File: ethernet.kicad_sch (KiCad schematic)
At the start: 20 parts, among them U6 RTL8211F-CG

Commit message: sch-eth-usb-updated
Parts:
- added C809: 4u7, Capacitor_SMD:C_0402_1005Metric, symbol Device:C
- added C810, C811: 100n, Capacitor_SMD:C_0402_1005Metric, symbol Device:C
- added J800: HR911130A, HR911130A, symbol Schematic-Lib-PhilsLab:HR911130A
- added L800: 3uh3, Inductor_SMD:L_0603_1608Metric, symbol Device:L
- added R800, R801, R804, R818, R819, R820: 4K7, Resistor_SMD:R_0402_1005Metric, symbol Device:R
- added R802: DNP_4K7, Resistor_SMD:R_0402_1005Metric, symbol Device:R
- added R803, R805, R806, R813, R814: 1k, Resistor_SMD:R_0402_1005Metric, symbol Device:R
- added R807, R808, R809, R810, R811, R812, R815, R816, R817: 22R, Resistor_SMD:R_0402_1005Metric, symbol Device:R
- added R821: 2K49, Resistor_SMD:R_0402_1005Metric, symbol Device:R
- added R822, R823: 510, Resistor_SMD:R_0402_1005Metric, symbol Device:R
- added X800: ECS-2520MV-250, XTAL_2520, symbol Schematic-Lib-PhilsLab:ECS-2520MV-130-BN-TR
- renumbered U6 to U800
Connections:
- net +1V0_ETH: now also C809.1, C810.1, L800.2
- net +1V8_ETH: now also C811.1, R800.2, R801.2, R802.2, R804.2, R813.2, R814.2, X800.1 (EN), X800.4 (VDD)
- net +3V3: now also J800.11 (LED_GREEN_A), J800.14 (LED_YELLOW_A), R818.1, R820.1
- net GND: now also C809.2, C810.2, C811.2, J800.10 (GND), R803.1, R805.1, R806.1, R816.2, R819.2, R821.2, X800.2 (GND)
- net MDI0_P: now reaches U800.1 (MDIP0)
- net MDI0_P: now also J800.2 (MD0+)
- net MDI3_N: now reaches U800.10 (MDIN3)
- net MDI3_N: now also J800.9 (MD3-)
- net ETH_NRST_+3V3: now reaches U800.12 (PHYRSTB)
- net ETH_MDC: now reaches U800.13 (MDC)
- net ETH_MDIO: now reaches U800.14 (MDIO)
- net ETH_MDIO: now also R814.1
- net ETH_PHY_TXD3: now reaches U800.15 (TXD3)
- net ETH_PHY_TXD2: now reaches U800.16 (TXD2)
- net ETH_PHY_TXD1: now reaches U800.17 (TXD1)
- net ETH_PHY_TXD0: now reaches U800.18 (TXD0)
- net ETH_PHY_TXCTL: now reaches U800.19 (TXCTL)
- net MDI0_N: now reaches U800.2 (MDIN0)
- net MDI0_N: now also J800.3 (MD0-)
- net ETH_PHY_TXCLK: now reaches U800.20 (TXC)
- net ETH_PHY_RXD3: now reaches U800.22 (RXD3/PHYAD0)
- net ETH_PHY_RXD3: now also R810.1
- net ETH_PHY_RXD2: now reaches U800.23 (RXD2/PLLOFF)
- net ETH_PHY_RXD2: now also R809.1
- net ETH_PHY_RXD1: now reaches U800.24 (RXD1/TXDLY)
- net ETH_PHY_RXD1: now also R808.1
- net ETH_PHY_RXD0: now reaches U800.25 (RXD0/RXDLY)
- net ETH_PHY_RXD0: now also R807.1
- net ETH_PHY_RXCTL: now reaches U800.26 (RXCTL/PHYAD2)
- net ETH_PHY_RXCTL: now also R811.1
- net ETH_PHY_RXCLK: now reaches U800.27 (RXC/PHYAD1)
- net ETH_PHY_RXCLK: now also R812.1
- net at U800.30 (REG_OUT/LDO_OUT): now also L800.1
- net ETH_NINT: now reaches U800.31 (INTB/PMEB)
- net ETH_NINT: now also R813.1
- net ETH_LED0: now reaches U800.32 (LED0/CFG_EXT)
- net ETH_LED0: now also R818.2, R822.2
- net ETH_LED1: now reaches U800.33 (LED1/CFG_LDO0)
- net ETH_LED1: now also R819.1
- net ETH_LED2: now reaches U800.34 (LED2/CFG_LDO1)
- net ETH_LED2: now also R820.2, R823.2
- net ETH_CLKOUT: now reaches U800.35 (CLKOUT)
- net ETH_CLKOUT: now also R817.1
- net at U800.36 (XTAL_IN): now also R816.1
- net ETH_CLK_25MHZ: now reaches U800.37 (XTAL_OUT/EXT_CLK)
- net ETH_CLK_25MHZ: now also R815.1
- net ETH_RSET: now reaches U800.39 (RSET)
- net ETH_RSET: now also R821.1
- net MDI1_P: now reaches U800.4 (MDIP1)
- net MDI1_P: now also J800.4 (MD1+)
- net MDI1_N: now reaches U800.5 (MDIN1)
- net MDI1_N: now also J800.7 (MD1-)
- net MDI2_P: now reaches U800.6 (MDIP2)
- net MDI2_P: now also J800.5 (MD2+)
- net MDI2_N: now reaches U800.7 (MDIN2)
- net MDI2_N: now also J800.6 (MD2-)
- net MDI3_P: now reaches U800.9 (MDIP3)
- net MDI3_P: now also J800.8 (MD3+)
- new net CGND: J800.SH (SHIELD)
- new net CLK_25MHZ: R815.2, X800.3 (OUT)
- new net ETH_LED_GR_K: J800.12 (LED_GREEN_K), R822.1
- new net ETH_LED_YL_A: J800.13 (LED_YELLOW_K), R823.1
- new net ETH_RXCLK: R806.2, R812.2
- new net ETH_RXCTL: R805.2, R811.2
- new net ETH_RXD0: R800.1, R807.2
- new net ETH_RXD1: R801.1, R808.2
- new net ETH_RXD2: R802.1, R803.2, R809.2
- new net ETH_RXD3: R804.1, R810.2
- new net PL_CLK_125MHZ: R817.2
- no-connect marks 0 -> 1
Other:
- note added: "Diff pair"
- note added: "GIGABIT ETHERNET"
- moved on the sheet: C807, C808

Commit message: all page
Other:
- title: (none) -> (text "GIGABIT ETHERNET" (exclude_from_sim no)
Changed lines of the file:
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@@
 	(generator_version "8.0")
 	(paper "A4")
+	(title_block
+		(title "(text \"GIGABIT ETHERNET\" (exclude_from_sim no)")
+		(date "2024-12-05")
+	)
 	(junction
 		(at 166.37 58.42)
@@
 	(wire
 		(pts
+			(xy 82.55 116.84) (xy 107.95 116.84)
+		)
+		(stroke
+			(width 0)
+			(type default)
+		)
+	)
+	(wire
+		(pts
 			(xy 276.86 71.12) (xy 276.86 111.76)
 		)
@@
 		(pts
 			(xy 29.21 71.12) (xy 50.8 71.12)
-		)
-		(stroke
-			(width 0)
-			(type default)
-		)
-	)
-	(wire
-		(pts
-			(xy 85.09 116.84) (xy 107.95 116.84)
 		)
 		(stroke
@@
 		)
 	)
-	(label "ETH_NRST_+3V3"
-		(at 85.09 116.84 0)
-		(fields_autoplaced yes)
-		(effects
-			(font
-				(size 1.016 1.016)
-				(thickness 0.127)
-			)
-			(justify left bottom)
-		)
-	)
 	(label "ETH_LED_GR_K"
 		(at 243.84 111.76 0)
@@
 		)
 	)
+	(global_label "ETH_NRST_+3V3"
+		(shape input)
+		(at 82.55 116.84 180)
+		(fields_autoplaced yes)
+		(effects
+			(font
+				(size 1.016 1.016)
+				(thickness 0.254)
+				(bold yes)
+			)
+			(justify right)
+		)
+		(property "Intersheetrefs" "${INTERSHEET_REFS}"
+			(at 67.3351 116.84 0)
+			(effects
+				(font
+					(size 1.27 1.27)
+				)
+				(justify right)
+				(hide yes)
+			)
+		)
+	)

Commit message: all page
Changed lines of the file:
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@@
 	(wire
 		(pts
-			(xy 88.9 96.52) (xy 107.95 96.52)
+			(xy 99.06 96.52) (xy 107.95 96.52)
 		)
 		(stroke
@@
 	(wire
 		(pts
-			(xy 88.9 93.98) (xy 107.95 93.98)
+			(xy 99.06 93.98) (xy 107.95 93.98)
 		)
 		(stroke
@@
 	(wire
 		(pts
-			(xy 88.9 88.9) (xy 107.95 88.9)
+			(xy 99.06 88.9) (xy 107.95 88.9)
 		)
 		(stroke
@@
 	(wire
 		(pts
-			(xy 88.9 86.36) (xy 107.95 86.36)
+			(xy 99.06 86.36) (xy 107.95 86.36)
 		)
 		(stroke
@@
 	(wire
 		(pts
-			(xy 73.66 129.54) (xy 91.44 129.54)
+			(xy 80.01 129.54) (xy 91.44 129.54)
 		)
 		(stroke
@@
 	(wire
 		(pts
-			(xy 88.9 91.44) (xy 107.95 91.44)
+			(xy 99.06 91.44) (xy 107.95 91.44)
 		)
 		(stroke
@@
 	(wire
 		(pts
-			(xy 88.9 99.06) (xy 107.95 99.06)
+			(xy 99.06 99.06) (xy 107.95 99.06)
 		)
 		(stroke
@@
 		)
 	)
-	(label "ETH_PHY_TXCTL"
-		(at 88.9 96.52 0)
-		(fields_autoplaced yes)
-		(effects
-			(font
-				(size 1.016 1.016)
-				(thickness 0.127)
-			)
-			(justify left bottom)
-		)
-	)
 	(label "ETH_NINT"
 		(at 85.09 111.76 0)
@@
 		)
 	)
-	(label "ETH_PHY_TXD3"
-		(at 88.9 93.98 0)
-		(fields_autoplaced yes)
-		(effects
-			(font
-				(size 1.016 1.016)
-			)
-			(justify left bottom)
-		)
-	)
-	(label "ETH_PHY_TXD2"
-		(at 88.9 91.44 0)
-		(fields_autoplaced yes)
-		(effects
-			(font
-				(size 1.016 1.016)
-			)
-			(justify left bottom)
-		)
-	)
 	(label "MDI2_N"
 		(at 191.77 86.36 0)
@@
 		)
 	)
-	(label "ETH_PHY_TXD1"
-		(at 88.9 88.9 0)
-		(fields_autoplaced yes)
-		(effects
-			(font
-				(size 1.016 1.016)
-			)
-			(justify left bottom)
-		)
-	)
 	(label "ETH_LED_GR_K"
 		(at 243.84 111.76 0)
@@
 		)
 	)
-	(label "PL_CLK_125MHZ"
-		(at 73.66 129.54 0)
-		(fields_autoplaced yes)
-		(effects
-			(font
-				(size 1.016 1.016)
-				(thickness 0.127)
-			)
-			(justify left bottom)
-		)
-	)
 	(label "MDI1_P"
 		(at 191.77 76.2 0)
@@
 		)
 	)
-	(label "ETH_PHY_TXD0"
-		(at 88.9 86.36 0)
-		(fields_autoplaced yes)
-		(effects
-			(font
-				(size 1.016 1.016)
-			)
-			(justify left bottom)
-		)
-	)
-	(label "ETH_PHY_TXCLK"
-		(at 88.9 99.06 0)
-		(fields_autoplaced yes)
-		(effects
-			(font
-				(size 1.016 1.016)
-				(thickness 0.127)
-			)
-			(justify left bottom)
-		)
-	)
 	(label "ETH_RXD0"
 		(at 29.21 68.58 0)
@@
 		)
 	)
-	(label "ETH_MDC"
-		(at 90.17 106.68 0)
-		(fields_autoplaced yes)
-		(effects
-			(font
-				(size 1.016 1.016)
-				(thickness 0.127)
-			)
-			(justify left bottom)
-		)
-	)
 	(label "ETH_LED1"
 		(at 190.5 109.22 0)
@@
 			)
 			(justify left bottom)
+		)
+	)
+	(global_label "PL_CLK_125MHZ"
+		(shape input)
+		(at 80.01 129.54 180)
+		(fields_autoplaced yes)
+		(effects
+			(font
+				(size 1.016 1.016)
+				(thickness 0.254)
+				(bold yes)
+			)
+			(justify right)
+		)
+		(property "Intersheetrefs" "${INTERSHEET_REFS}"
+			(at 64.65 129.54 0)
+			(effects
+				(font
+					(size 1.27 1.27)
+				)
+				(justify right)
+				(hide yes)
+			)
+		)
+	)
+	(global_label "ETH_PHY_TXCTL"
+		(shape input)
+		(at 99.06 96.52 180)
+		(fields_autoplaced yes)
+		(effects
+			(font
+				(size 0.762 0.762)
+				(thickness 0.254)
+				(bold yes)
+			)
+			(justify right)
+		)
+		(property "Intersheetrefs" "${INTERSHEET_REFS}"
+			(at 88.0839 96.52 0)
+			(effects
+				(font
+					(size 1.27 1.27)
+				)
+				(justify right)
+				(hide yes)
+			)
+		)
+	)
+	(global_label "ETH_MDC"
+		(shape input)
+		(at 90.17 106.68 180)
+		(fields_autoplaced yes)
+		(effects
+			(font
+				(size 0.762 0.762)
+				(thickness 0.254)
+				(bold yes)
+			)
+			(justify right)
+		)
+		(property "Intersheetrefs" "${INTERSHEET_REFS}"
+			(at 82.8588 106.68 0)
+			(effects
+				(font
+					(size 1.27 1.27)
+				)
+				(justify right)
+				(hide yes)
+			)
+		)
+	)
+	(global_label "ETH_PHY_TXD1"
+		(shape input)
+		(at 99.06 88.9 180)
+		(fields_autoplaced yes)
+		(effects
+			(font
+				(size 0.762 0.762)
+				(thickness 0.254)
+				(bold yes)
+			)
+			(justify right)
+		)
+		(property "Intersheetrefs" "${INTERSHEET_REFS}"
+			(at 88.5557 88.9 0)
+			(effects
+				(font
+					(size 1.27 1.27)
+				)
+				(justify right)
+				(hide yes)
+			)
+		)
+	)
+	(global_label "ETH_PHY_TXD0"
+		(shape input)
+		(at 99.06 86.36 180)
+		(fields_autoplaced yes)
+		(effects
+			(font
+				(size 0.762 0.762)
+				(thickness 0.254)
+				(bold yes)
+			)
+			(justify right)
+		)
+		(property "Intersheetrefs" "${INTERSHEET_REFS}"
+			(at 88.5557 86.36 0)
+			(effects
+				(font
+					(size 1.27 1.27)
+				)
+				(justify right)
+				(hide yes)
+			)
+		)
+	)
+	(global_label "ETH_PHY_TXD2"
+		(shape input)
+		(at 99.06 91.44 180)
+		(fields_autoplaced yes)
+		(effects
+			(font
+				(size 0.762 0.762)
+				(thickness 0.254)
+				(bold yes)
+			)
+			(justify right)
+		)
+		(property "Intersheetrefs" "${INTERSHEET_REFS}"
+			(at 88.5557 91.44 0)
+			(effects
+				(font
+					(size 1.27 1.27)
+				)
+				(justify right)
+				(hide yes)
+			)
 		)
 	)
@@
 			(effects
 				(font
+					(size 1.27 1.27)
+				)
+				(justify right)
+				(hide yes)
+			)
+		)
+	)
+	(global_label "ETH_PHY_TXD3"
+		(shape input)
+		(at 99.06 93.98 180)
+		(fields_autoplaced yes)
+		(effects
+			(font
+				(size 0.762 0.762)
+				(thickness 0.254)
+				(bold yes)
+			)
+			(justify right)
+		)
+		(property "Intersheetrefs" "${INTERSHEET_REFS}"
+			(at 88.5557 93.98 0)
+			(effects
+				(font
+					(size 1.27 1.27)
+				)
+				(justify right)
+				(hide yes)
+			)
+		)
+	)
+	(global_label "ETH_PHY_TXCLK"
+		(shape input)
+		(at 99.06 99.06 180)
+		(fields_autoplaced yes)
+		(effects
+			(font
+				(size 0.762 0.762)
+				(thickness 0.254)
+				(bold yes)
+			)
+			(justify right)
+		)
+		(property "Intersheetrefs" "${INTERSHEET_REFS}"
+			(at 87.9025 99.06 0)
+			(effects
+				(font

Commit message: sch-to-pcb
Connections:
- net ETH_REG_OUT: now reaches L800.1, U800.30 (REG_OUT/LDO_OUT)
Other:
- moved on the sheet: R814

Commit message: ram-update
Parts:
- FB800, FB801: footprint FB_0402 -> Footprint-Lib-PhilsLab:FB_0402
- J800: footprint HR911130A -> Footprint-Lib-PhilsLab:HR911130A
- X800: footprint XTAL_2520 -> Footprint-Lib-PhilsLab:XTAL_2520
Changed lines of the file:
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@@
 			)
 		)
-		(property "Footprint" "HR911130A"
+		(property "Footprint" "Footprint-Lib-PhilsLab:HR911130A"
 			(at 251.46 81.28 0)
 			(effects
@@
 			)
 		)
-		(property "Footprint" "FB_0402"
+		(property "Footprint" "Footprint-Lib-PhilsLab:FB_0402"
 			(at 50.8 43.18 0)
 			(effects
@@
 			)
 		)
-		(property "Footprint" "FB_0402"
+		(property "Footprint" "Footprint-Lib-PhilsLab:FB_0402"
 			(at 231.14 38.1 0)
 			(effects
@@
 			)
 		)
-		(property "Footprint" "XTAL_2520"
+		(property "Footprint" "Footprint-Lib-PhilsLab:XTAL_2520"
 			(at 38.1 124.46 0)
 			(effects

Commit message: ram-zynq-updated
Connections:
- net MDI3_N renamed MDI4_N
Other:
- note added: "ETH_MDI"
- note added: "RGMII_RX_PHY"
- note added: "RGMII_TX_PHY"

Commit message: pcb_eth
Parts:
- U800: footprint Footprint-Lib-PhilsLab:QFN-40-0.4-EP -> easyeda2kicad_foorprint:WQFN-40_L5.0-W5.0-P0.4-BL-EP; LCSC (none) -> C187932
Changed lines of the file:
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@@
 			)
 		)
-		(property "Footprint" "Footprint-Lib-PhilsLab:QFN-40-0.4-EP"
+		(property "Footprint" "easyeda2kicad_foorprint:WQFN-40_L5.0-W5.0-P0.4-BL-EP"
 			(at 148.59 99.06 0)
 			(effects
@@
 				(hide yes)
 			)
+		)
+		(property "LCSC" "C187932"
+			(at 148.59 99.06 0)
+			(effects
+				(font
+					(size 1.27 1.27)
+				)
+				(hide yes)
+			)

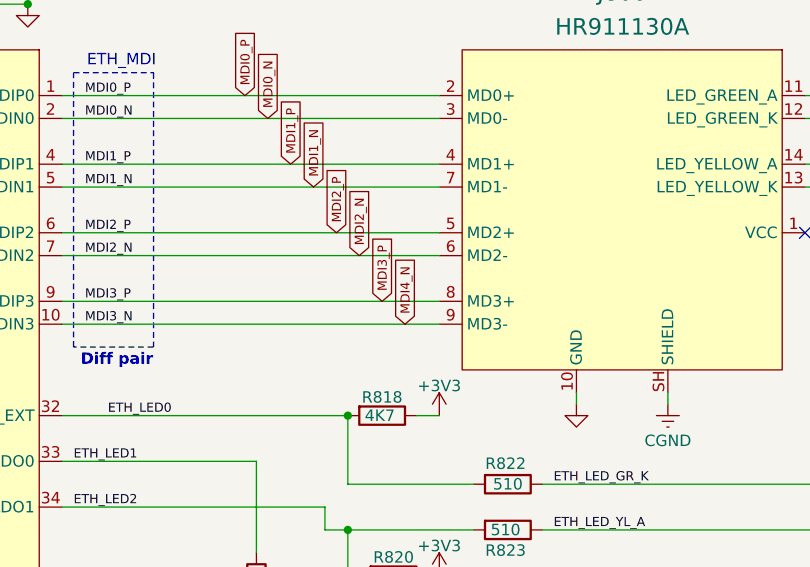
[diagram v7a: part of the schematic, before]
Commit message: usb hs update
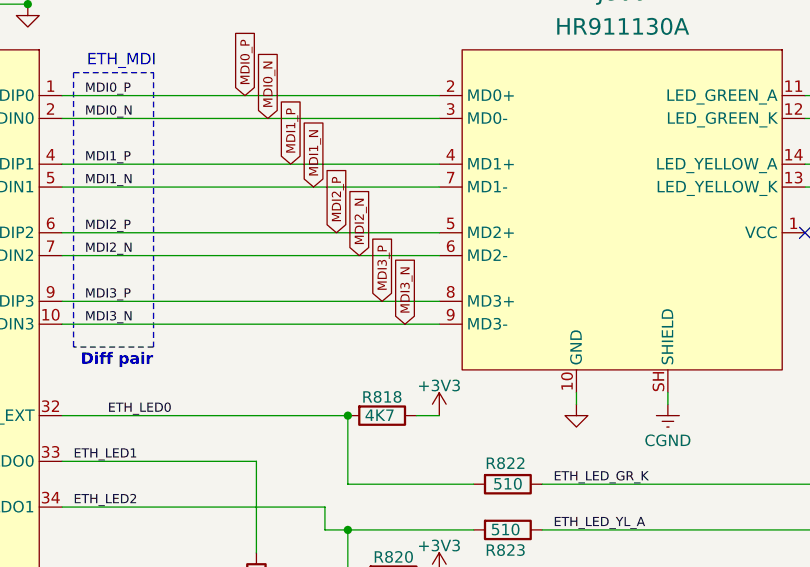
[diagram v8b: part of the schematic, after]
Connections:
- net MDI4_N renamed MDI3_N
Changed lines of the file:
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@@
 		)
 	)
-	(global_label "MDI4_N"
+	(global_label "MDI3_N"
 		(shape input)
 		(at 227.33 93.98 90)
